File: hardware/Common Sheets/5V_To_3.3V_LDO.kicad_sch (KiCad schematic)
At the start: 3 parts, among them U2 TLV71333PDBV

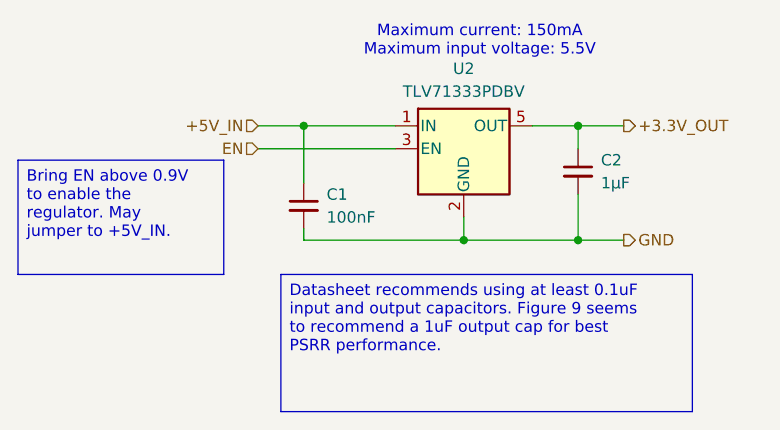
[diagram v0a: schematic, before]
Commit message: Add schematic for Vsupply input
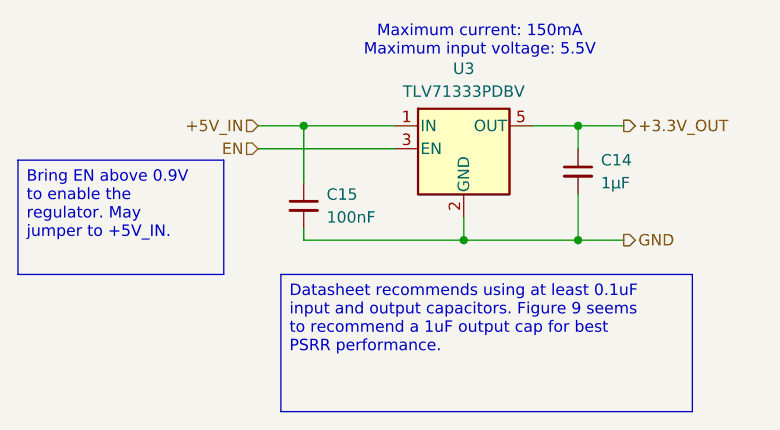
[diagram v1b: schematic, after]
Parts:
- renumbered C2 to C14, C1 to C15, U2 to U3
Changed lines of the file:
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@@
 		(dnp no)
 		(fields_autoplaced yes)
-		(property "Reference" "U2"
+		(property "Reference" "U3"
 			(at 74.93 44.45 0)
 			(effects
@@
 		(dnp no)
 		(fields_autoplaced yes)
-		(property "Reference" "C2"
+		(property "Reference" "C14"
 			(at 90.17 54.6162 0)
 			(effects
@@
 		(dnp no)
 		(fields_autoplaced yes)
-		(property "Reference" "C1"
+		(property "Reference" "C15"
 			(at 59.69 58.4262 0)
 			(effects

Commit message: Route more of main unit, start on KiBot CI job
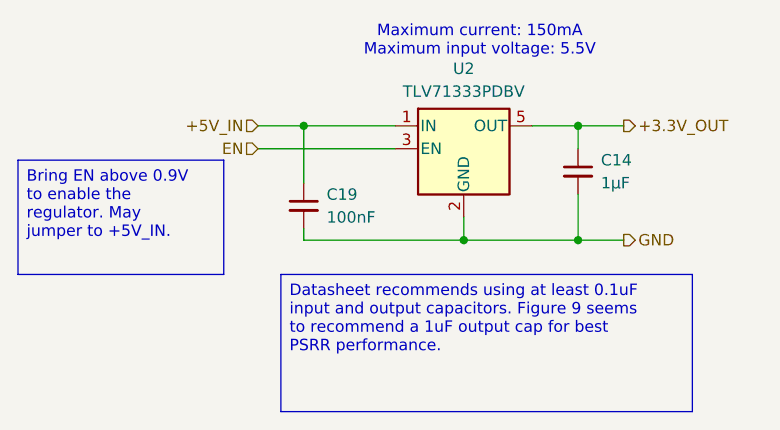
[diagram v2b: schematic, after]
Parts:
- renumbered C15 to C19, U3 to U2
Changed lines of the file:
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@@
 		(dnp no)
 		(fields_autoplaced yes)
-		(property "Reference" "U3"
+		(property "Reference" "U2"
 			(at 74.93 44.45 0)
 			(effects
@@
 			(project "HackerDAQ Voltage Card"
 				(path "/af2d881c-6553-449d-9093-6deb41497bdc/8683fa8f-1b23-40d2-8dab-5a640e39446f"
-					(reference "U3")
+					(reference "U2")
 					(unit 1)
 				)
@@
 		(dnp no)
 		(fields_autoplaced yes)
-		(property "Reference" "C15"
+		(property "Reference" "C19"
 			(at 59.69 58.4262 0)
 			(effects
@@
 			(project "HackerDAQ Voltage Card"
 				(path "/af2d881c-6553-449d-9093-6deb41497bdc/8683fa8f-1b23-40d2-8dab-5a640e39446f"
-					(reference "C15")
-					(unit 1)
-				)
+					(reference "C19")
+					(unit 1)
+				)

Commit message: Add Main Unit to CI build as well
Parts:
- C14: LibRef (none) -> CL10B105MO8NNWC
- C19: LibRef (none) -> ESD35C104K4T2A-24
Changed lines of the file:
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@@
+			)
+		)
+		(property "LibRef" "CL10B105MO8NNWC"
+			(at 87.63 55.88 0)
+			(effects
+				(font
+					(size 1.27 1.27)
+				)
+				(hide yes)
 			)
 		)
@@
 			(at 57.15 59.69 0)
 			(effects
+				(font
+					(size 1.27 1.27)
+				)
+				(hide yes)
+			)
+		)
+		(property "LibRef" "ESD35C104K4T2A-24"
+			(at 57.15 59.69 0)
+			(effects

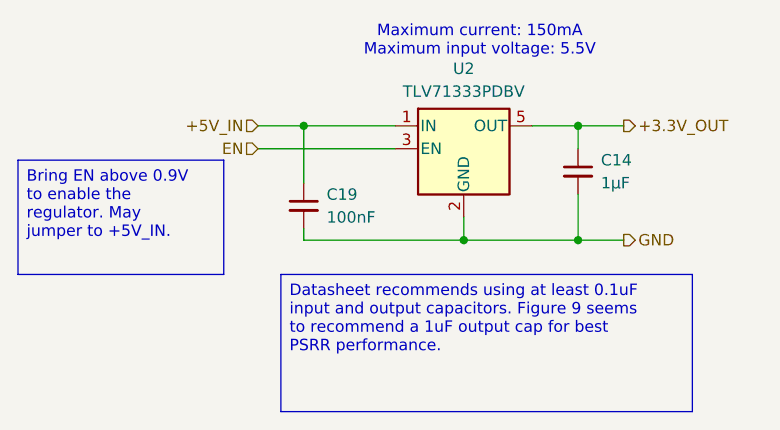
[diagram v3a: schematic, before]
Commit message: Add LEDs and 5V regulator to main unit
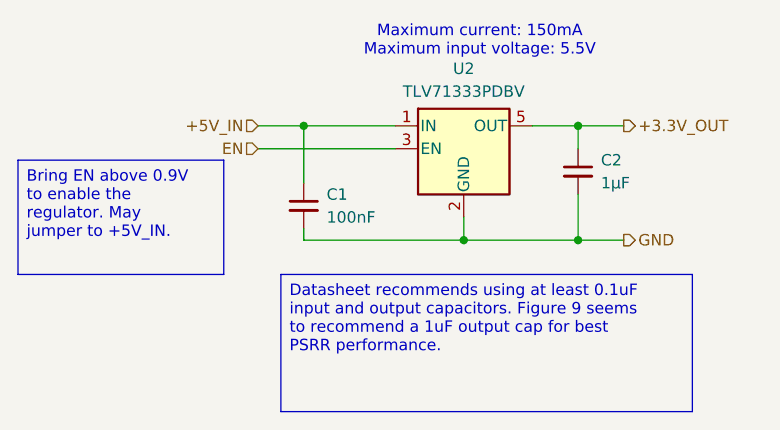
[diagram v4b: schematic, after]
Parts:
- renumbered C19 to C1, C14 to C2
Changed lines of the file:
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@@
 		)
 		(instances
-			(project "Main Unit"
+			(project "HackerDAQ Main Unit"
 				(path "/7d91f165-331a-4c48-9d02-ee2a0aa7e94a/e7d4db02-ae45-49ee-8383-9be3f30124de"
 					(reference "U2")
@@
 		(dnp no)
 		(fields_autoplaced yes)
-		(property "Reference" "C14"
+		(property "Reference" "C2"
 			(at 90.17 54.6162 0)
 			(effects
@@
 		)
 		(instances
-			(project "Main Unit"
+			(project "HackerDAQ Main Unit"
 				(path "/7d91f165-331a-4c48-9d02-ee2a0aa7e94a/e7d4db02-ae45-49ee-8383-9be3f30124de"
 					(reference "C2")
@@
 		(dnp no)
 		(fields_autoplaced yes)
-		(property "Reference" "C19"
+		(property "Reference" "C1"
 			(at 59.69 58.4262 0)
 			(effects
@@
 		)
 		(instances
-			(project "Main Unit"
+			(project "HackerDAQ Main Unit"
 				(path "/7d91f165-331a-4c48-9d02-ee2a0aa7e94a/e7d4db02-ae45-49ee-8383-9be3f30124de"
 					(reference "C1")

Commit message: Geographical reannotate
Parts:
- renumbered C2 to C3, C1 to C4
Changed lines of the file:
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@@
 		(dnp no)
 		(fields_autoplaced yes)
-		(property "Reference" "C2"
+		(property "Reference" "C3"
 			(at 90.17 54.6162 0)
 			(effects
@@
 			(project "HackerDAQ Main Unit"
 				(path "/7d91f165-331a-4c48-9d02-ee2a0aa7e94a/e7d4db02-ae45-49ee-8383-9be3f30124de"
-					(reference "C2")
+					(reference "C3")
 					(unit 1)
 				)
@@
 		(dnp no)
 		(fields_autoplaced yes)
-		(property "Reference" "C1"
+		(property "Reference" "C4"
 			(at 59.69 58.4262 0)
 			(effects
@@
 			(project "HackerDAQ Main Unit"
 				(path "/7d91f165-331a-4c48-9d02-ee2a0aa7e94a/e7d4db02-ae45-49ee-8383-9be3f30124de"
-					(reference "C1")
+					(reference "C4")
 					(unit 1)
 				)
